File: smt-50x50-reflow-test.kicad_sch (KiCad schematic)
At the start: 104 parts, among them J1 Conn_01x04_Pin, J2 Conn_01x02, J3 Conn_01x01, J4 USB_C_Receptacle_USB2.0_14P, J5 Conn_01x01, J6 Conn_01x01, J7 Conn_01x01, J8 Conn_01x04_Pin, J9 Conn_01x03_Pin, SW1 SW_Push, SW2 SW_Push, U1 ESP32-C6, U14 TMP117AIDRV, U15 BMP581, U16 TMP117AIDRV, U2 W25Q128JVS, U3 AP2112K-3.3, U4 LM317_TO-252, U5 LMR36520FADDA, U7 USBLC6-2SC6, Y1 48M

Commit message: schem: remove one TMP117 alert line
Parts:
- removed R62: 10k, Resistor_SMD:R_0603_1608Metric, symbol Device:R
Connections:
- net TMP117_ALERT2: no longer names the net of U16.3 (ALERT)
- net TMP117_ALERT2: no longer U1.36 (GPIO23/SDIO_DATA3)
- no-connect marks 8 -> 10
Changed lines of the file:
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@@
 	)
 	(no_connect
+		(at 265.43 31.75)
+	)
+	(no_connect
 		(at 138.43 73.66)
 	)
@@
 		(at 138.43 86.36)
 	)
+	(no_connect
+		(at 138.43 106.68)
+	)
 	(wire
 		(pts
@@
 	(wire
 		(pts
-			(xy 273.05 30.48) (xy 273.05 31.75)
-		)
-		(stroke
-			(width 0)
-			(type default)
-		)
-	)
-	(wire
-		(pts
 			(xy 162.56 80.01) (xy 162.56 78.74)
 		)
@@
 	(wire
 		(pts
-			(xy 138.43 106.68) (xy 154.94 106.68)
-		)
-		(stroke
-			(width 0)
-			(type default)
-		)
-	)
-	(wire
-		(pts
 			(xy 187.96 90.17) (xy 187.96 96.52)
 		)
@@
 	(wire
 		(pts
-			(xy 265.43 31.75) (xy 273.05 31.75)
-		)
-		(stroke
-			(width 0)
-			(type default)
-		)
-	)
-	(wire
-		(pts
 			(xy 265.43 132.08) (xy 264.16 132.08)
 		)
@@
 	(wire
 		(pts
-			(xy 273.05 21.59) (xy 273.05 22.86)
-		)
-		(stroke
-			(width 0)
-			(type default)
-		)
-	)
-	(wire
-		(pts
 			(xy 203.2 95.25) (xy 205.74 95.25)
 		)
@@
 		)
 	)
-	(label "TMP117_ALERT2"
-		(at 271.78 31.75 270)
-		(effects
-			(font
-				(size 1.27 1.27)
-			)
-			(justify right bottom)
-		)
-	)
 	(label "RF_ESP"
 		(at 63.5 39.37 0)
@@
 		)
 	)
-	(label "TMP117_ALERT2"
-		(at 154.94 106.68 180)
-		(effects
-			(font
-				(size 1.27 1.27)
-			)
-			(justify right bottom)
-		)
-	)
 	(label "SDA"
 		(at 151.13 78.74 180)
@@
 	)
 	(symbol
-		(lib_id "Device:R")
-		(at 273.05 26.67 0)
-		(unit 1)
-		(exclude_from_sim no)
-		(in_bom yes)
-		(on_board yes)
-		(dnp no)
-		(fields_autoplaced yes)
-		(property "Reference" "R62"
-			(at 275.59 25.3999 0)
-			(effects
-				(font
-					(size 1.27 1.27)
-				)
-				(justify left)
-			)
-		)
-		(property "Value" "10k"
-			(at 275.59 27.9399 0)
-			(effects
-				(font
-					(size 1.27 1.27)
-				)
-				(justify left)
-			)
-		)
-		(property "Footprint" "Resistor_SMD:R_0603_1608Metric"
-			(at 271.272 26.67 90)
-			(effects
-				(font
-					(size 1.27 1.27)
-				)
-				(hide yes)
-			)
-		)
-		(property "Datasheet" "~"
-			(at 273.05 26.67 0)
-			(effects
-				(font
-					(size 1.27 1.27)
-				)
-				(hide yes)
-			)
-		)
-		(property "Description" "Resistor"
-			(at 273.05 26.67 0)
-			(effects
-				(font
-					(size 1.27 1.27)
-				)
-				(hide yes)
-			)
-		)
-		(property "Basic" "Y"
-			(at 273.05 26.67 0)
-			(effects
-				(font
-					(size 1.27 1.27)
-				)
-				(hide yes)
-			)
-		)
-		(property "JLCPCB Part #" "C25804"
-			(at 273.05 26.67 0)
-			(effects
-				(font
-					(size 1.27 1.27)
-				)
-				(hide yes)
-			)
-		)
-		(property "Manufacturer" "Uniroyal Elec"
-			(at 273.05 26.67 0)
-			(effects
-				(font
-					(size 1.27 1.27)
-				)
-				(hide yes)
-			)
-		)
-		(property "Manufacturer Part Number" "0603WAF1002T5E"
-			(at 273.05 26.67 0)
-			(effects
-				(font
-					(size 1.27 1.27)
-				)
-				(hide yes)
-			)
-		)
-		(pin "1"
-		)
-		(pin "2"
-		)
-		(instances
-			(project "smt-50x50-reflow-test"
-				(path "/316df49b-410f-46a7-9063-0920c2d0517b"
-					(reference "R62")
-					(unit 1)
-				)
-			)
-		)
-	)
-	(symbol
 		(lib_id "Device:C")
 		(at 62.23 45.72 0)
@@
 					(unit 1)
 				)
-			)
-		)
-	)
-	(symbol
-		(lib_id "power:+3V3")
-		(at 273.05 21.59 0)
-		(unit 1)
-		(exclude_from_sim no)
-		(in_bom yes)
-		(on_board yes)
-		(dnp no)
-		(property "Reference" "#PWR0110"
-			(at 273.05 25.4 0)
-			(effects
-				(font
-					(size 1.27 1.27)
-				)
-				(hide yes)
-			)
-		)
-		(property "Value" "+3V3"
-			(at 270.51 17.272 0)
-			(effects
-				(font
-					(size 1.27 1.27)
-				)
-				(justify left)
-			)
-		)
-		(property "Footprint" ""
-			(at 273.05 21.59 0)
-			(effects
-				(font
-					(size 1.27 1.27)
-				)
-				(hide yes)
-			)
-		)
-		(property "Datasheet" ""
-			(at 273.05 21.59 0)
-			(effects
-				(font
-					(size 1.27 1.27)
-				)
-				(hide yes)
-			)
-		)
-		(property "Description" "Power symbol creates a global label with name \"+3V3\""
-			(at 273.05 21.59 0)
-			(effects
-				(font
-					(size 1.27 1.27)
-				)
-				(hide yes)
-			)
-		)
-		(pin "1"
-		)
-		(instances
-			(project "smt-50x50-reflow-test"
-				(path "/316df49b-410f-46a7-9063-0920c2d0517b"
-					(reference "#PWR0110")
-					(unit 1)
-				)

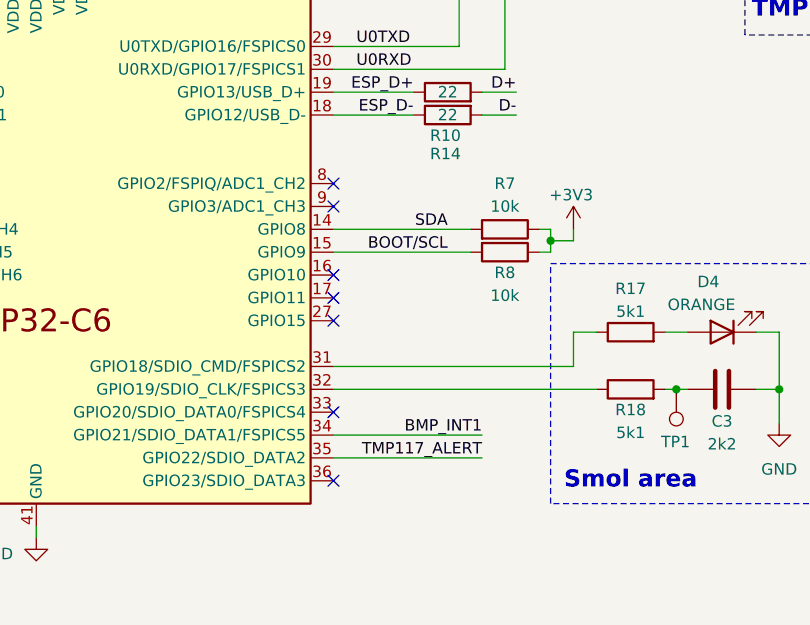
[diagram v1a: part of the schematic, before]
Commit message: pcb: route TMP117 and BMP581 interrupts
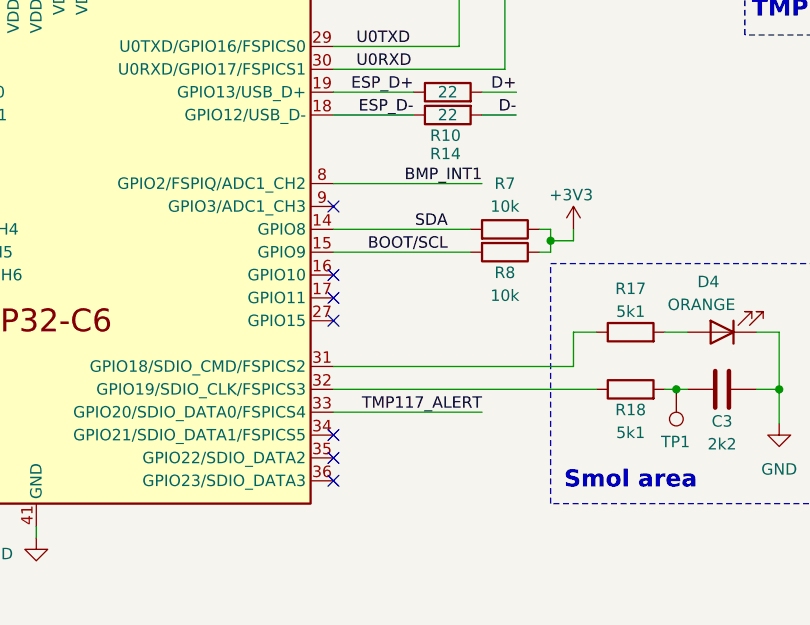
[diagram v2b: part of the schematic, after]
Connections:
- net BMP_INT1: now also U1.8 (GPIO2/FSPIQ/ADC1_CH2); no longer U1.34 (GPIO21/SDIO_DATA1/FSPICS5)
- net TMP117_ALERT: now also U1.33 (GPIO20/SDIO_DATA0/FSPICS4); no longer U1.35 (GPIO22/SDIO_DATA2)
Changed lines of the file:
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@@
 	)
 	(no_connect
-		(at 138.43 99.06)
-	)
-	(no_connect
 		(at 138.43 83.82)
 	)
@@
 	)
 	(no_connect
-		(at 138.43 73.66)
+		(at 138.43 104.14)
 	)
 	(no_connect
@@
 		(at 138.43 106.68)
 	)
+	(no_connect
+		(at 138.43 101.6)
+	)
 	(wire
 		(pts
@@
 	(wire
 		(pts
-			(xy 138.43 101.6) (xy 154.94 101.6)
-		)
-		(stroke
-			(width 0)
-			(type default)
-		)
-	)
-	(wire
-		(pts
 			(xy 96.52 144.78) (xy 96.52 142.24)
 		)
@@
 	(wire
 		(pts
-			(xy 138.43 104.14) (xy 154.94 104.14)
-		)
-		(stroke
-			(width 0)
-			(type default)
-		)
-	)
-	(wire
-		(pts
 			(xy 59.69 39.37) (xy 62.23 39.37)
 		)
@@
 	(wire
 		(pts
+			(xy 138.43 73.66) (xy 154.94 73.66)
+		)
+		(stroke
+			(width 0)
+			(type default)
+		)
+	)
+	(wire
+		(pts
 			(xy 60.96 134.62) (xy 62.23 134.62)
 		)
@@
 	(wire
 		(pts
+			(xy 138.43 99.06) (xy 154.94 99.06)
+		)
+		(stroke
+			(width 0)
+			(type default)
+		)
+	)
+	(wire
+		(pts
 			(xy 62.23 146.05) (xy 62.23 144.78)
 		)
@@
 		)
 	)
-	(label "TMP117_ALERT"
-		(at 154.94 104.14 180)
-		(effects
-			(font
-				(size 1.27 1.27)
-			)
-			(justify right bottom)
-		)
-	)
 	(label "BOOT{slash}SCL"
 		(at 242.57 74.93 0)
@@
 		)
 	)
-	(label "BMP_INT1"
-		(at 154.94 101.6 180)
-		(effects
-			(font
-				(size 1.27 1.27)
-			)
-			(justify right bottom)
-		)
-	)
 	(label "SDA"
 		(at 247.65 77.47 0)
@@
 		(effects
 			(font
+				(size 1.27 1.27)
+			)
+			(justify right bottom)
+		)
+	)
+	(label "BMP_INT1"
+		(at 154.94 73.66 180)
+		(effects
+			(font
+				(size 1.27 1.27)
+			)
+			(justify right bottom)
+		)
+	)
+	(label "TMP117_ALERT"
+		(at 154.94 99.06 180)
+		(effects
+			(font

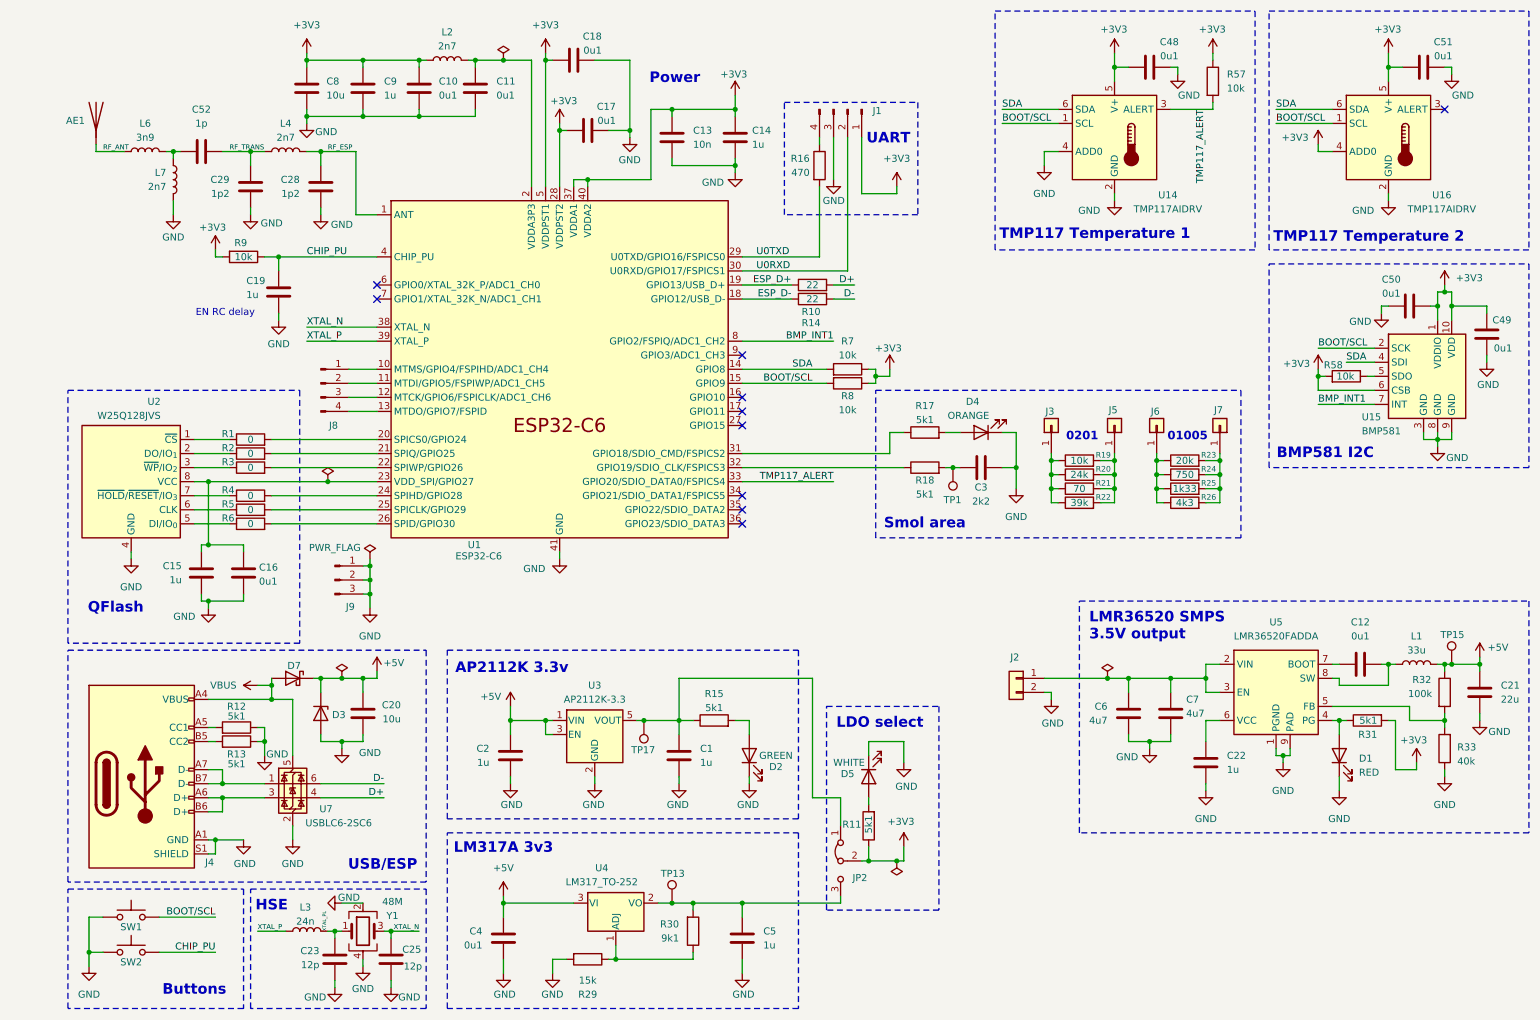
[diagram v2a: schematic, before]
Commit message: pcb(silkscreen): add user info
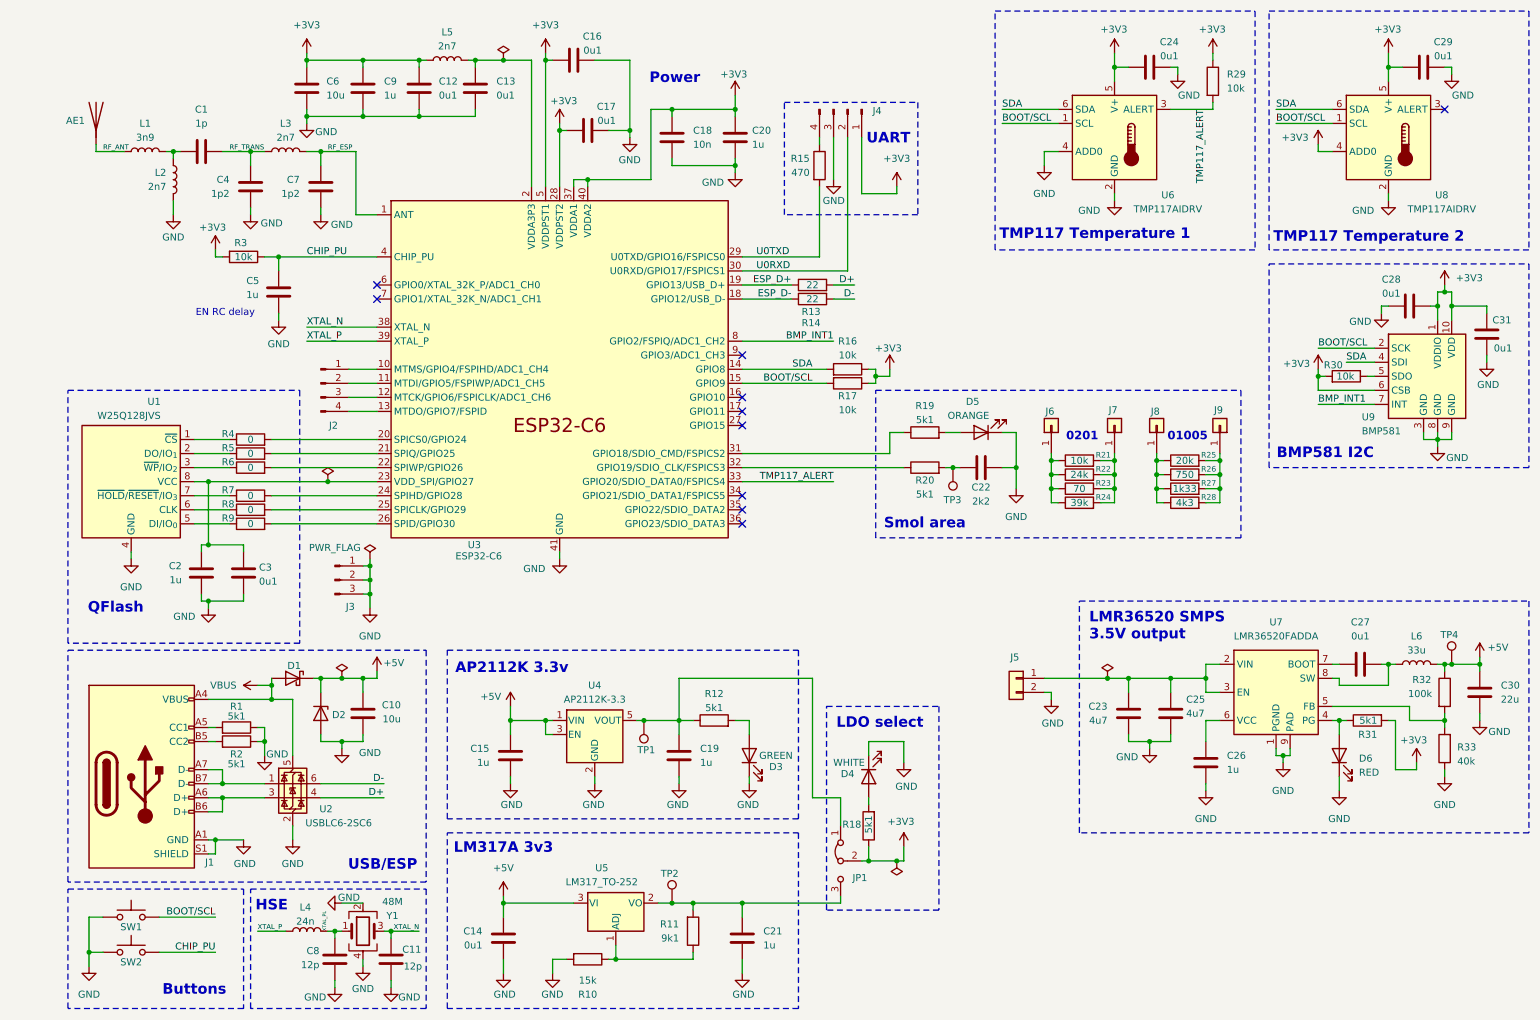
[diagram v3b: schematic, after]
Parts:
- renumbered C52 to C1, C20 to C10, C25 to C11, C10 to C12, C11 to C13, C4 to C14, C2 to C15, C18 to C16, C13 to C18, C1 to C19, C15 to C2, C14 to C20, C5 to C21, C3 to C22, C6 to C23, C48 to C24, C7 to C25, C22 to C26, C12 to C27, C50 to C28, C51 to C29, C16 to C3, C21 to C30, C49 to C31, C29 to C4, C19 to C5, C8 to C6, C28 to C7, C23 to C8, D7 to D1, D3 to D2, D2 to D3, D5 to D4, D4 to D5, D1 to D6, J4 to J1, J8 to J2, J9 to J3, J1 to J4, J2 to J5, J3 to J6, J5 to J7, J6 to J8, J7 to J9, JP2 to JP1, L6 to L1, L7 to L2, L4 to L3, L3 to L4, L2 to L5, L1 to L6, R12 to R1, R29 to R10, R30 to R11, R15 to R12, R10 to R13, R16 to R15, R7 to R16, R8 to R17, R11 to R18, R17 to R19, R13 to R2, R18 to R20, R19 to R21, R20 to R22, R21 to R23, R22 to R24, R23 to R25, R24 to R26, R25 to R27, R26 to R28, R57 to R29, R9 to R3, R58 to R30, R1 to R4, R2 to R5, R3 to R6, R4 to R7, R5 to R8, R6 to R9, TP17 to TP1, TP13 to TP2, TP1 to TP3, TP15 to TP4, U2 to U1, U7 to U2, U1 to U3, U3 to U4, U4 to U5, U14 to U6, U5 to U7, U16 to U8, U15 to U9

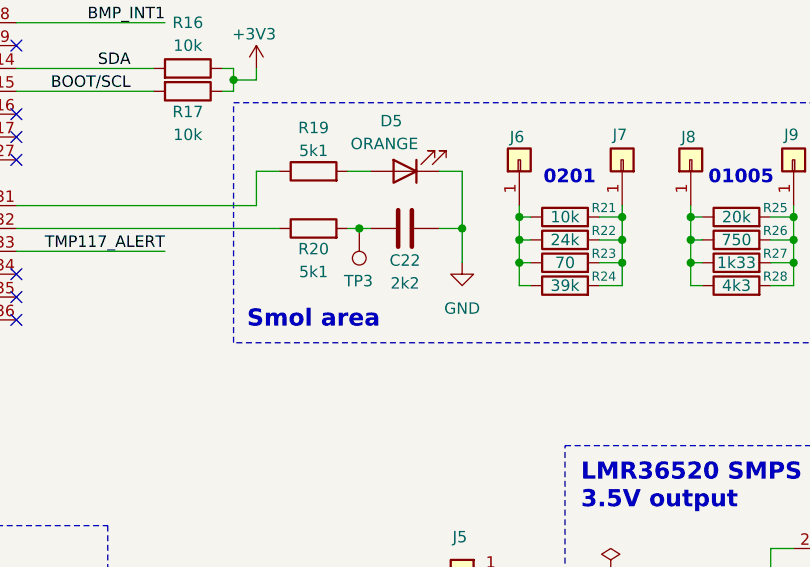
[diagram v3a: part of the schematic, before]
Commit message: schem: add missing BOM info
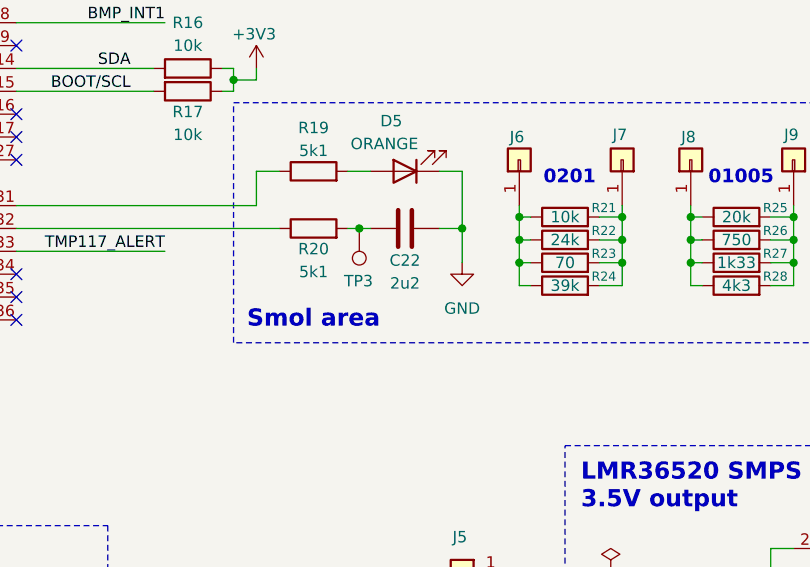
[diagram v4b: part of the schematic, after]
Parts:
- C22: value 2k2 -> 2u2; JLCPCB Part # (none) -> C335106; Manufacturer (none) -> Murata; Manufacturer Part Number (none) -> GRM033R61A225KE47D
- D5: JLCPCB Part # (none) -> C5440629; Manufacturer (none) -> XINGLIGHT; Manufacturer Part Number (none) -> XL-0201UOC
- R19, R20: JLCPCB Part # (none) -> C270344; Manufacturer (none) -> Uniroyal Elec; Manufacturer Part Number (none) -> 0201WMF5101TEE
- R21: JLCPCB Part # (none) -> C473048; Manufacturer (none) -> Uniroyal Elec; Manufacturer Part Number (none) -> 0201WMF1002TEE C473048
- R22: JLCPCB Part # (none) -> C270353; Manufacturer (none) -> Uniroyal Elec; Manufacturer Part Number (none) -> 0201WMF2402TEE
- R23: JLCPCB Part # (none) -> C270692; Manufacturer (none) -> Uniroyal Elec; Manufacturer Part Number (none) -> 0201WMF698JTEE
- R24: JLCPCB Part # (none) -> C473053; Manufacturer (none) -> Uniroyal Elec; Manufacturer Part Number (none) -> 0201WMF3902TEE
- R25: JLCPCB Part # (none) -> C560400; Manufacturer (none) -> Uniroyal Elec; Manufacturer Part Number (none) -> 0105WHJ0203TDE
- R26: JLCPCB Part # (none) -> C850442; Manufacturer (none) -> YAGEO; Manufacturer Part Number (none) -> RC0100FR-07750RL
- R27: JLCPCB Part # (none) -> C507485; Manufacturer (none) -> ROHM; Manufacturer Part Number (none) -> MCR004QLPF1331
- R28: JLCPCB Part # (none) -> C560366; Manufacturer (none) -> Uniroyal Elec; Manufacturer Part Number (none) -> 0105WHF4301TDE
